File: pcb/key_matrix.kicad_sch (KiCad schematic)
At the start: 108 parts, among them SW1 SW_Push, SW10 SW_Push, SW11 SW_Push, SW12 SW_Push, SW13 SW_Push, SW14 SW_Push, SW15 SW_Push, SW16 SW_Push, SW17 SW_Push, SW18 SW_Push, SW19 SW_Push, SW2 SW_Push, SW20 SW_Push, SW21 SW_Push, SW22 SW_Push, SW23 SW_Push, SW24 SW_Push, SW25 SW_Push, SW26 SW_Push, SW27 SW_Push, SW28 SW_Push, SW29 SW_Push, SW3 SW_Push, SW30 SW_Push, SW31 SW_Push, SW32 SW_Push, SW33 SW_Push, SW34 SW_Push, SW35 SW_Push, SW36 SW_Push, SW37 SW_Push, SW38 SW_Push, SW39 SW_Push, SW4 SW_Push, SW40 SW_Push, SW41 SW_Push, SW42 SW_Push, SW43 SW_Push, SW44 SW_Push, SW45 SW_Push, SW46 SW_Push, SW47 SW_Push, SW48 SW_Push, SW49 SW_Push, SW5 SW_Push, SW50 SW_Push, SW51 SW_Push, SW52 SW_Push, SW53 SW_Push, SW54 SW_Push, SW55 SW_Push, SW56 SW_Push, SW6 SW_Push, SW7 SW_Push, SW8 SW_Push, SW9 SW_Push

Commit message: updated bom
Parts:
- D1, D10, D11, D12, D13, D14, D15, D16, D17, D18, D19, D2, D20, D21, D22, D23, D24, D25, D26, D27, D28, D29, D3, D30, D31, D32, D33, D34, D35, D36, D37, D38, D39, D4, D40, D41, D42, D43, D44, D45, D46, D47, D48, D49, D5, D50, D51, D52, D6, D7, D8, D9: LCSC C81598 -> (none)

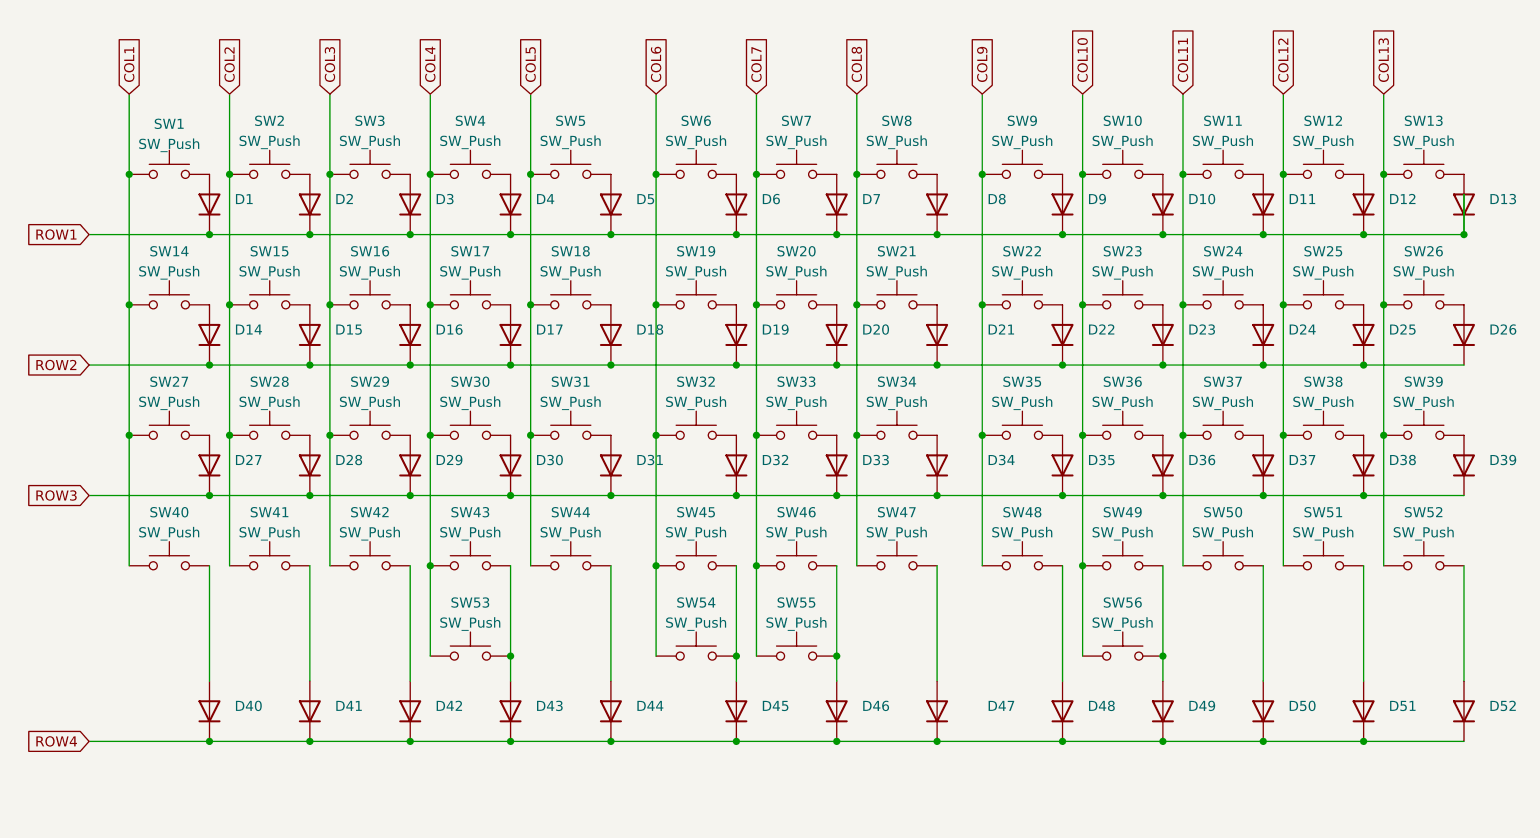
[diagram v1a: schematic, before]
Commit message: Added 150/225 bottom row for hhkb support
Fixed positions of many bottom row alternate layouts. No BOM changes, just moved one diode and a few conflicting traces.
Gerbers have been updated
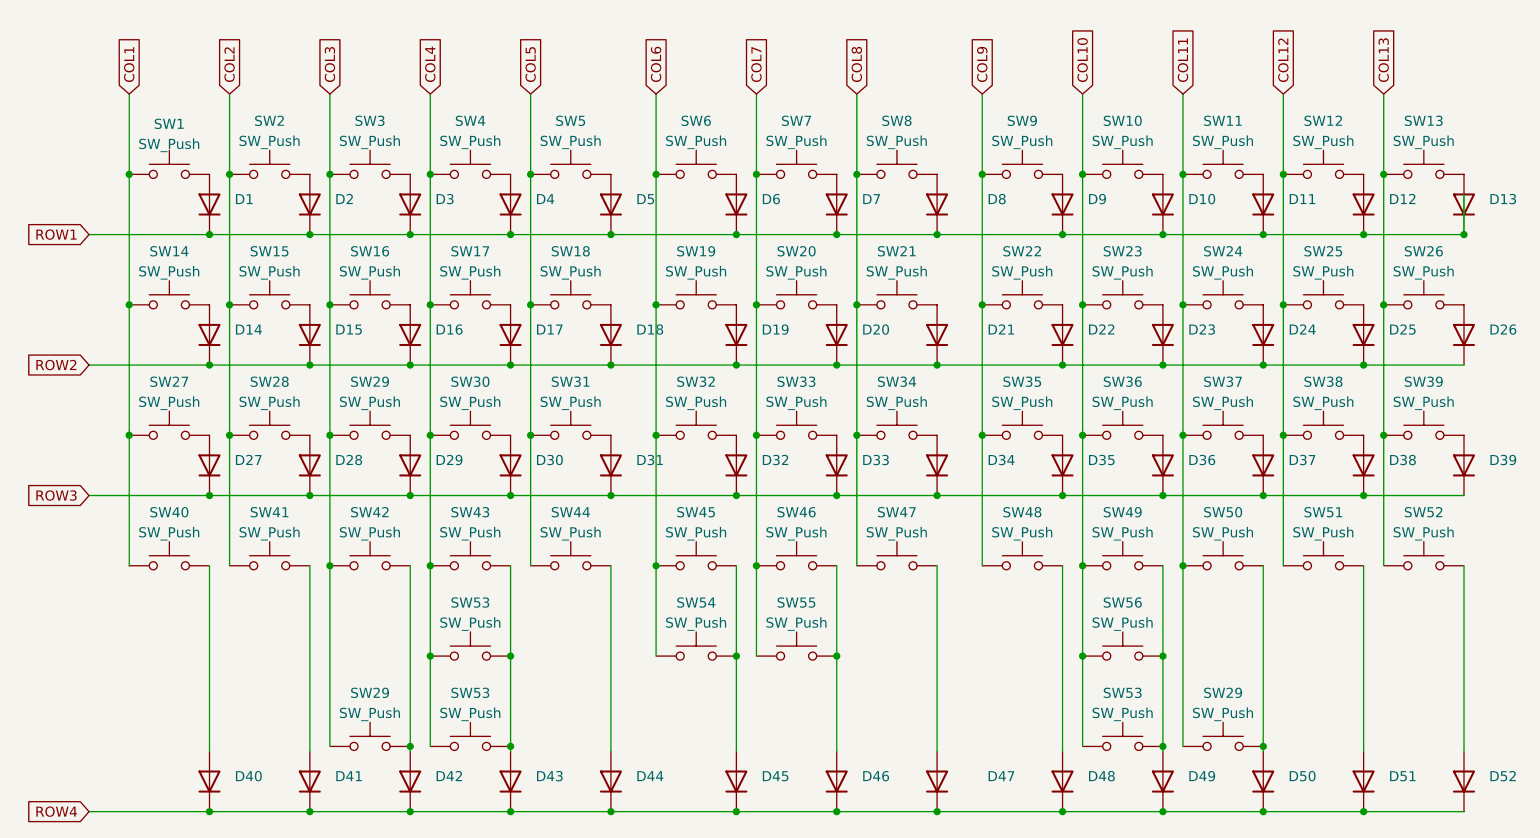
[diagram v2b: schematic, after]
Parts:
- added SW29 (x2): SW_Push, MX_Solderable:MX-Solderable-1.5U, symbol Switch:SW_Push
- added SW53 (x2): SW_Push, MX_Solderable:MX-Solderable-2.25U-ReversedStabilizers, symbol Switch:SW_Push
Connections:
- net COL10: now also SW56.2, SW53.2; no longer SW56.1
- net COL11: now also SW29.1
- net COL3: now also SW29.1
- net COL4: now also SW53.2, SW53.2; no longer SW53.1
- net at D43.2 (A), SW43.2: now also SW53.1, SW53.1; no longer SW53.2
- net at D49.2 (A), SW49.2: now also SW56.1, SW53.1; no longer SW56.2
- net at D50.2 (A), SW50.2: now also SW29.2
- net at D42.2 (A), SW42.2: now also SW29.2
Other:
- moved on the sheet: D40, D41, D42, D43, D44, D45, D46, D47, D48, D49, D50, D51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
